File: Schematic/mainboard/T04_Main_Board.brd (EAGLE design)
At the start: 78.2 x 33.3 mm, 21 parts, among them IC1 7805DT, J1 AVR_SPI_PRG_6PTH, U1 ATMEGA328P_PDIP

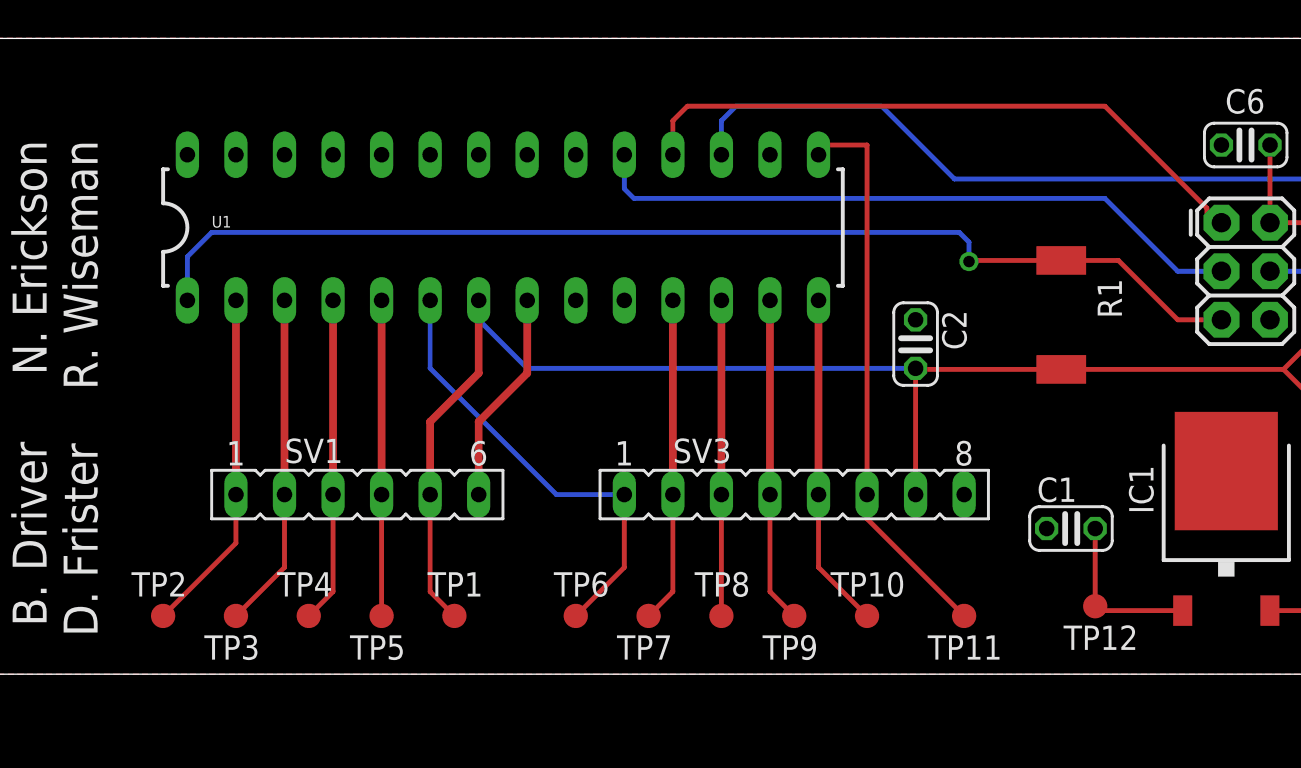
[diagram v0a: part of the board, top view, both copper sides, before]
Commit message: Mainboard update - Clock and bypass caps
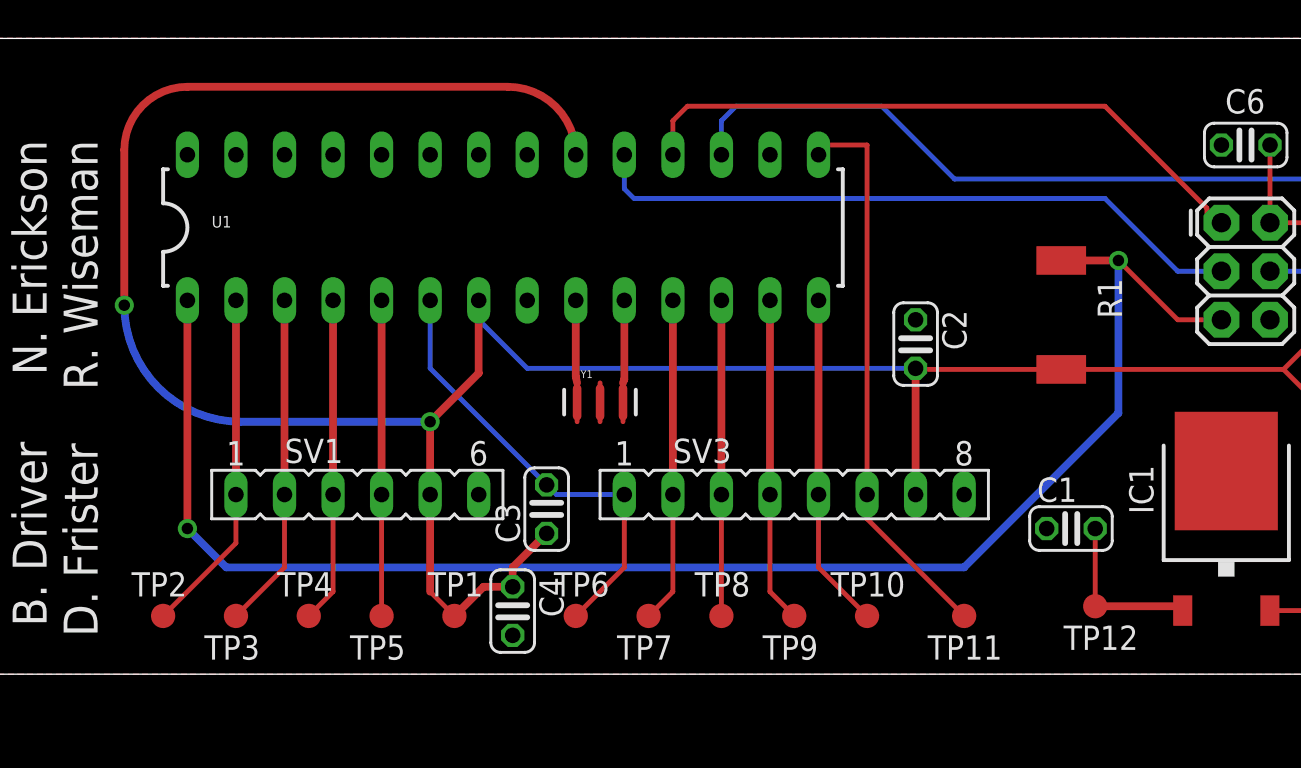
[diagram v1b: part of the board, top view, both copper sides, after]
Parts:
- added C3, C4: 0.1u, rcl:C025-024X044
- added Y1: 16MHZ, SparkFun-FreqCtrl:RESONATOR-SMD
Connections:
- new net N$1: U1.9, Y1.1
- new net N$2: U1.10, Y1.3
- new net N$3: Y1.2
- net +5V: now also C3.1, C4.1, U1.20
- net GND: now also C3.2, C4.2
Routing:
- net +5V: track 101.7 -> 162.0 mm, vias 0 -> 2
- net RESET: track 59.4 -> 82.5 mm, vias 1 -> 2
- net GND: track 10.7 -> 0.00 mm
- net N$2: track 0.00 -> 4.33 mm
- net N$1: track 0.00 -> 4.33 mm
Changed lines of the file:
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@@
 </element>
 <element name="U1" library="SparkFun-DigitalIC" package="DIL28-3" value="ATMEGA328P_PDIP" x="30.988" y="23.368"/>
+<element name="C3" library="rcl" package="C025-024X044" value="0.1u" x="33.274" y="8.636" rot="R90"/>
+<element name="C4" library="rcl" package="C025-024X044" value="0.1u" x="31.496" y="3.302" rot="R270"/>
+<element name="Y1" library="SparkFun-FreqCtrl" package="RESONATOR-SMD" value="16MHZ" x="36.068" y="14.224">
+<attribute name="PROD_ID" value="XTAL-08900" x="36.068" y="14.224" size="1.778" layer="27" display="off"/>
+</element>
 </elements>
 <signals>
@@
 <contactref element="J1" pad="6"/>
 <contactref element="C6" pad="2"/>
-<contactref element="SV1" pad="6"/>
 <contactref element="U1" pad="8"/>
 <contactref element="U1" pad="22"/>
-<contactref element="SV3" pad="8"/>
-<wire x1="29.718" y1="9.398" x2="29.464" y2="9.652" width="0.4064" layer="1"/>
-<wire x1="29.464" y1="9.652" x2="29.718" y2="9.906" width="0.4064" layer="1"/>
-<wire x1="29.718" y1="9.906" x2="29.718" y2="13.208" width="0.4064" layer="1"/>
-<wire x1="29.718" y1="13.208" x2="32.258" y2="15.748" width="0.4064" layer="1"/>
-<wire x1="32.258" y1="15.748" x2="32.258" y2="18.796" width="0.4064" layer="1"/>
 <polygon width="0.254" layer="1" isolate="0.3048">
 <vertex x="0" y="0"/>
@@
 <vertex x="78.232" y="0"/>
 </polygon>
+<contactref element="C3" pad="2"/>
+<contactref element="SV3" pad="8"/>
+<contactref element="C4" pad="2"/>
+<contactref element="SV1" pad="6"/>
 </signal>
 <signal name="+5V">
@@
 <contactref element="TP1" pad="TP"/>
 <contactref element="J1" pad="2"/>
-<contactref element="SV1" pad="5"/>
 <contactref element="C6" pad="1"/>
-<contactref element="SV3" pad="7"/>
 <contactref element="U1" pad="7"/>
-<wire x1="27.178" y1="9.398" x2="27.178" y2="13.208" width="0.4064" layer="1"/>
 <wire x1="27.178" y1="13.208" x2="29.718" y2="15.748" width="0.4064" layer="1"/>
 <wire x1="29.718" y1="15.748" x2="29.718" y2="19.558" width="0.4064" layer="1"/>
-<wire x1="27.178" y1="9.398" x2="27.178" y2="4.318" width="0.254" layer="1"/>
 <wire x1="27.178" y1="4.318" x2="28.448" y2="3.048" width="0.254" layer="1"/>
 <wire x1="60.198" y1="15.946" x2="71.826" y2="15.946" width="0.254" layer="1"/>
@@
 <wire x1="60.198" y1="15.946" x2="52.634" y2="15.946" width="0.254" layer="1"/>
 <wire x1="52.634" y1="15.946" x2="52.578" y2="16.002" width="0.254" layer="1"/>
-<wire x1="52.578" y1="9.398" x2="52.578" y2="16.002" width="0.254" layer="1"/>
 <wire x1="71.12" y1="27.686" x2="71.12" y2="24.384" width="0.254" layer="1"/>
 <wire x1="71.12" y1="24.384" x2="71.374" y2="24.13" width="0.254" layer="1"/>
@@
 <wire x1="32.258" y1="16.002" x2="29.718" y2="18.542" width="0.254" layer="16"/>
 <wire x1="29.718" y1="18.542" x2="29.718" y2="19.558" width="0.254" layer="16"/>
+<contactref element="C3" pad="1"/>
+<contactref element="SV3" pad="7"/>
+<contactref element="C4" pad="1"/>
+<contactref element="SV1" pad="5"/>
+<wire x1="52.578" y1="9.398" x2="52.578" y2="16.002" width="0.4064" layer="1"/>
+<wire x1="27.178" y1="13.208" x2="27.178" y2="9.398" width="0.4064" layer="1"/>
+<wire x1="27.178" y1="9.398" x2="27.178" y2="4.318" width="0.4064" layer="1"/>
+<wire x1="31.496" y1="4.572" x2="31.496" y2="5.588" width="0.4064" layer="1"/>
+<wire x1="31.496" y1="5.588" x2="33.274" y2="7.366" width="0.4064" layer="1"/>
+<wire x1="31.496" y1="4.572" x2="29.972" y2="4.572" width="0.4064" layer="1"/>
+<wire x1="29.972" y1="4.572" x2="28.448" y2="3.048" width="0.4064" layer="1"/>
+<contactref element="U1" pad="20"/>
+<wire x1="34.798" y1="27.178" x2="31.242" y2="30.734" width="0.4064" layer="1" curve="90"/>
+<wire x1="31.242" y1="30.734" x2="14.478" y2="30.734" width="0.4064" layer="1"/>
+<wire x1="14.478" y1="30.734" x2="11.176" y2="27.432" width="0.4064" layer="1" curve="90"/>
+<wire x1="11.176" y1="27.432" x2="11.176" y2="19.304" width="0.4064" layer="1"/>
+<via x="11.176" y="19.304" extent="1-16" drill="0.6" shape="square"/>
+<wire x1="11.176" y1="19.304" x2="17.272" y2="13.208" width="0.4064" layer="16" curve="90"/>
+<wire x1="17.272" y1="13.208" x2="27.178" y2="13.208" width="0.4064" layer="16"/>
+<via x="27.178" y="13.208" extent="1-16" drill="0.6" shape="square"/>
 </signal>
 <signal name="+12V">
@@
 <contactref element="IC1" pad="1"/>
 <contactref element="TP12" pad="TP"/>
-<wire x1="61.976" y1="7.62" x2="61.976" y2="3.328" width="0.254" layer="1"/>
-<wire x1="61.976" y1="3.328" x2="66.554" y2="3.328" width="0.254" layer="1"/>
-<wire x1="61.976" y1="3.328" x2="61.976" y2="3.556" width="0" layer="19" extent="1-1"/>
+<wire x1="61.976" y1="7.62" x2="61.976" y2="3.556" width="0.254" layer="1"/>
+<wire x1="61.976" y1="3.556" x2="61.976" y2="3.328" width="0.254" layer="1"/>
+<wire x1="61.976" y1="3.556" x2="66.326" y2="3.556" width="0.4064" layer="1"/>
+<wire x1="66.326" y1="3.556" x2="66.554" y2="3.328" width="0.4064" layer="1"/>
 </signal>
 <signal name="RESET">
 <contactref element="J1" pad="5"/>
+<wire x1="63.19" y1="21.646" x2="66.294" y2="18.542" width="0.254" layer="1"/>
+<wire x1="66.294" y1="18.542" x2="68.58" y2="18.542" width="0.254" layer="1"/>
 <contactref element="R1" pad="1"/>
 <contactref element="U1" pad="1"/>
-<wire x1="60.198" y1="21.646" x2="63.19" y2="21.646" width="0.254" layer="1"/>
-<wire x1="63.19" y1="21.646" x2="66.294" y2="18.542" width="0.254" layer="1"/>
-<wire x1="66.294" y1="18.542" x2="68.58" y2="18.542" width="0.254" layer="1"/>
-<wire x1="60.198" y1="21.646" x2="55.428" y2="21.646" width="0.254" layer="1"/>
-<wire x1="55.428" y1="21.646" x2="55.372" y2="21.59" width="0.254" layer="1"/>
-<via x="55.372" y="21.59" extent="1-16" drill="0.6"/>
-<wire x1="55.372" y1="21.59" x2="55.372" y2="22.606" width="0.254" layer="16"/>
-<wire x1="55.372" y1="22.606" x2="54.864" y2="23.114" width="0.254" layer="16"/>
-<wire x1="54.864" y1="23.114" x2="15.748" y2="23.114" width="0.254" layer="16"/>
-<wire x1="15.748" y1="23.114" x2="14.478" y2="21.844" width="0.254" layer="16"/>
-<wire x1="14.478" y1="21.844" x2="14.478" y2="19.558" width="0.254" layer="16"/>
+<via x="63.19" y="21.646" extent="1-16" drill="0.6" shape="square"/>
+<wire x1="63.19" y1="21.646" x2="63.19" y2="13.66" width="0.4064" layer="16"/>
+<wire x1="63.19" y1="13.66" x2="55.118" y2="5.588" width="0.4064" layer="16"/>
+<wire x1="55.118" y1="5.588" x2="16.51" y2="5.588" width="0.4064" layer="16"/>
+<wire x1="16.51" y1="5.588" x2="14.478" y2="7.62" width="0.4064" layer="16"/>
+<via x="14.478" y="7.62" extent="1-16" drill="0.6" shape="square"/>
+<wire x1="14.478" y1="7.62" x2="14.478" y2="19.558" width="0.4064" layer="1"/>
+<wire x1="60.198" y1="21.646" x2="63.19" y2="21.646" width="0.4064" layer="1"/>
 </signal>
 <signal name="ECHO1">
@@
 <wire x1="27.178" y1="16.002" x2="27.178" y2="19.558" width="0.254" layer="16"/>
 </signal>
+<signal name="N$1">
+<contactref element="Y1" pad="1"/>
+<contactref element="U1" pad="9"/>
+<wire x1="34.798" y1="19.558" x2="34.798" y2="15.564" width="0.4064" layer="1"/>
+<wire x1="34.798" y1="15.564" x2="34.868" y2="15.24" width="0.4064" layer="1"/>
+</signal>
+<signal name="N$2">
+<contactref element="Y1" pad="3"/>
+<contactref element="U1" pad="10"/>
+<wire x1="37.338" y1="19.558" x2="37.338" y2="15.424" width="0.4064" layer="1"/>
+<wire x1="37.338" y1="15.424" x2="37.268" y2="15.24" width="0.4064" layer="1"/>
+</signal>
+<signal name="N$3">
+<contactref element="Y1" pad="2"/>
+</signal>
 </signals>

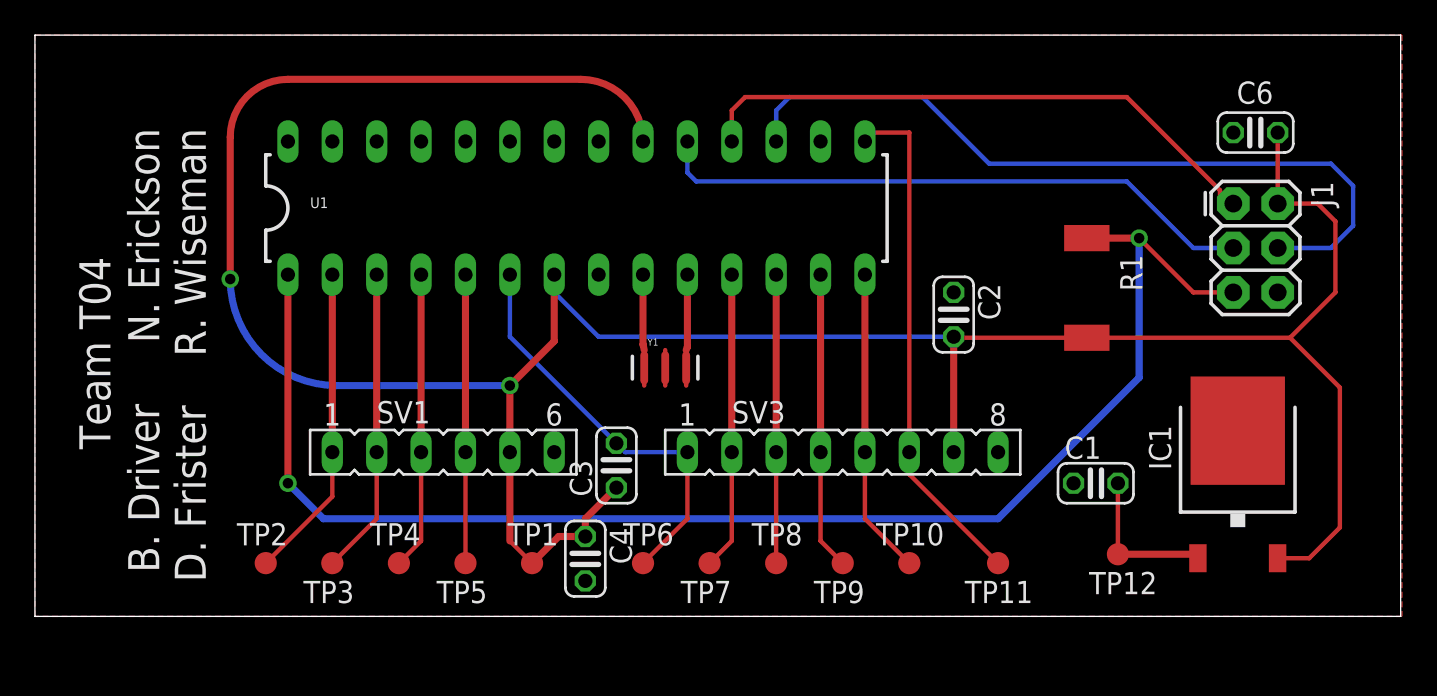
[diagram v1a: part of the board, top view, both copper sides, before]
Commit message: Mainboard - Added mounting holes
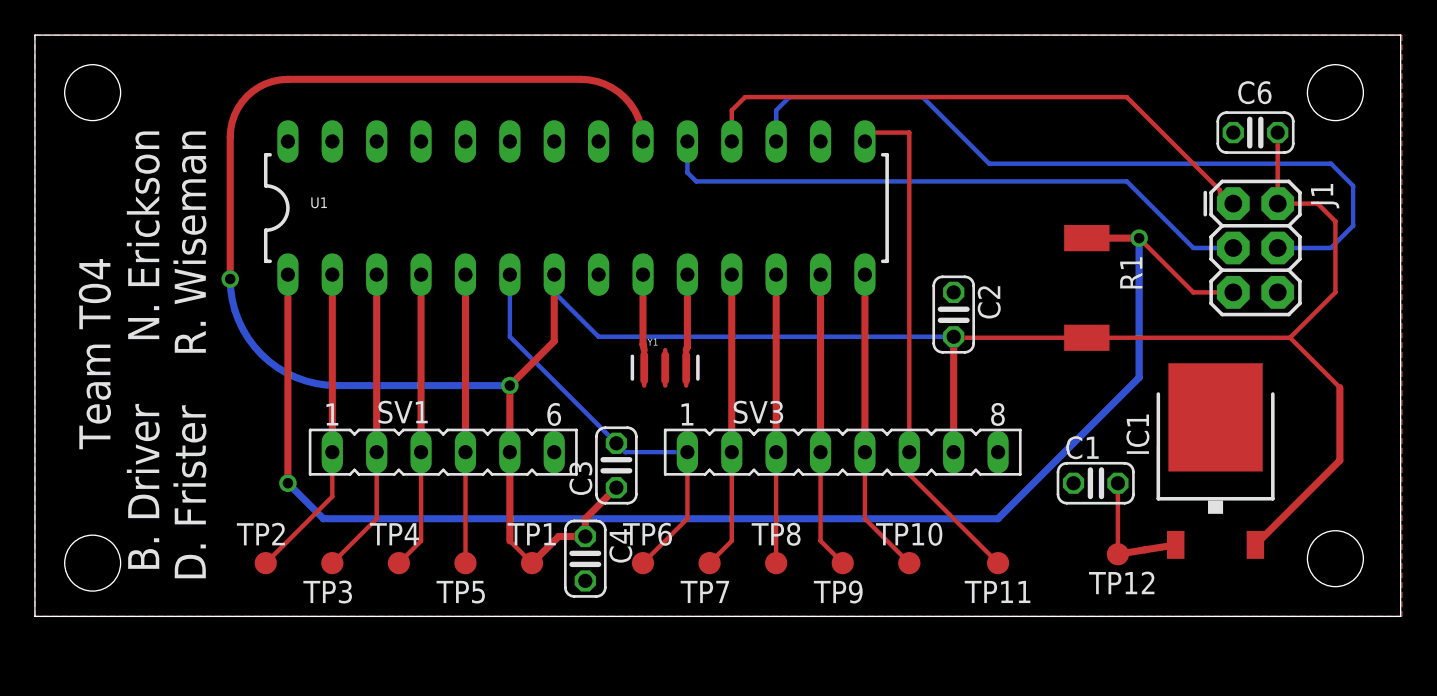
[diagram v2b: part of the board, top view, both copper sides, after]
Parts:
- moved IC1 1.48 mm to (67.6, 8.89)
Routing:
- net +12V: track 8.96 -> 7.64 mm
- net +5V: track 162.0 -> 160.7 mm
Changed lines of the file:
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@@
 <layer number="43" name="vRestrict" color="2" fill="10" visible="yes" active="yes"/>
 <layer number="44" name="Drills" color="7" fill="1" visible="no" active="yes"/>
-<layer number="45" name="Holes" color="7" fill="1" visible="no" active="yes"/>
+<layer number="45" name="Holes" color="7" fill="1" visible="yes" active="yes"/>
 <layer number="46" name="Milling" color="3" fill="1" visible="no" active="yes"/>
 <layer number="47" name="Measures" color="7" fill="1" visible="no" active="yes"/>
@@
 <text x="5.334" y="27.94" size="1.778" layer="25" rot="R270">B. Driver     N. Erickson
 D. Frister    R. Wiseman</text>
+<hole x="3.302" y="29.972" drill="3.2"/>
+<hole x="3.302" y="3.048" drill="3.2"/>
+<hole x="74.422" y="29.972" drill="3.2"/>
+<hole x="74.422" y="3.302" drill="3.2"/>
 </plain>
 <attributes>
@@
 <attribute name="VALUE" x="75.438" y="30.607" size="1.27" layer="27" ratio="10" rot="R180"/>
 </element>
-<element name="IC1" library="linear" package="TO252" value="7805DT" x="68.834" y="8.128" smashed="yes">
-<attribute name="NAME" x="65.024" y="8.382" size="1.27" layer="25" rot="R90"/>
-<attribute name="VALUE" x="73.914" y="5.588" size="1.27" layer="27" rot="R90"/>
+<element name="IC1" library="linear" package="TO252" value="7805DT" x="67.564" y="8.89" smashed="yes">
+<attribute name="NAME" x="63.754" y="9.144" size="1.27" layer="25" rot="R90"/>
+<attribute name="VALUE" x="72.644" y="6.35" size="1.27" layer="27" rot="R90"/>
 </element>
 <element name="J1" library="SparkFun-Connectors" package="2X3" value="AVR_SPI_PRG_6PTH" x="68.58" y="23.622" smashed="yes" rot="R270">
@@
 <wire x1="71.374" y1="24.13" x2="71.374" y2="23.876" width="0.254" layer="1"/>
 <wire x1="71.374" y1="23.876" x2="71.12" y2="23.622" width="0.254" layer="1"/>
-<wire x1="71.114" y1="3.328" x2="72.924" y2="3.328" width="0.254" layer="1"/>
-<wire x1="72.924" y1="3.328" x2="74.676" y2="5.08" width="0.254" layer="1"/>
-<wire x1="74.676" y1="5.08" x2="74.676" y2="13.096" width="0.254" layer="1"/>
 <wire x1="74.676" y1="13.096" x2="71.826" y2="15.946" width="0.254" layer="1"/>
 <wire x1="52.578" y1="16.002" x2="32.258" y2="16.002" width="0.254" layer="16"/>
@@
 <wire x1="17.272" y1="13.208" x2="27.178" y2="13.208" width="0.4064" layer="16"/>
 <via x="27.178" y="13.208" extent="1-16" drill="0.6" shape="square"/>
+<wire x1="74.676" y1="13.096" x2="74.676" y2="8.922" width="0.4064" layer="1"/>
+<wire x1="74.676" y1="8.922" x2="69.844" y2="4.09" width="0.4064" layer="1"/>
 </signal>
 <signal name="+12V">
@@
 <wire x1="61.976" y1="7.62" x2="61.976" y2="3.556" width="0.254" layer="1"/>
 <wire x1="61.976" y1="3.556" x2="61.976" y2="3.328" width="0.254" layer="1"/>
-<wire x1="61.976" y1="3.556" x2="66.326" y2="3.556" width="0.4064" layer="1"/>
-<wire x1="66.326" y1="3.556" x2="66.554" y2="3.328" width="0.4064" layer="1"/>
+<wire x1="61.976" y1="3.556" x2="63.532" y2="3.81" width="0.4064" layer="1"/>
+<wire x1="63.532" y1="3.81" x2="65.284" y2="4.09" width="0.4064" layer="1"/>
 </signal>
 <signal name="RESET">

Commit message: Fixed DRC errors on C3.
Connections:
- removed net GND: C1.1, C2.1, C3.2, C4.2, C6.2, IC1.3, J1.6, SV1.6, SV3.8, U1.22, U1.8
- removed net TRIG1: SV3.1, TP6.TP, U1.6
- new net S$1: C1.1, C2.1, C3.2, C4.2, C6.2, IC1.3, J1.6, SV1.6, SV3.1, SV3.8, TP6.TP, U1.22, U1.6, U1.8
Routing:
- net S$1: track 0.00 -> 30.7 mm
- net TRIG1: track 23.9 -> 0.00 mm
- added copper zone on layer 1, net S$1
- removed copper zone on layer 1, net GND
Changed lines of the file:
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@@
 </elements>
 <signals>
-<signal name="GND">
-<contactref element="IC1" pad="3"/>
-<contactref element="C1" pad="1"/>
-<contactref element="C2" pad="1"/>
-<contactref element="J1" pad="6"/>
-<contactref element="C6" pad="2"/>
-<contactref element="U1" pad="8"/>
-<contactref element="U1" pad="22"/>
-<polygon width="0.254" layer="1" isolate="0.3048">
-<vertex x="0" y="0"/>
-<vertex x="0" y="33.274"/>
-<vertex x="78.232" y="33.274"/>
-<vertex x="78.232" y="0"/>
-</polygon>
-<contactref element="C3" pad="2"/>
-<contactref element="SV3" pad="8"/>
-<contactref element="C4" pad="2"/>
-<contactref element="SV1" pad="6"/>
-</signal>
 <signal name="+5V">
 <contactref element="C2" pad="2"/>
@@
 <wire x1="47.498" y1="5.588" x2="50.038" y2="3.048" width="0.254" layer="1"/>
 </signal>
-<signal name="TRIG1">
+<signal name="S$1">
+<contactref element="U1" pad="6"/>
+<wire x1="27.178" y1="16.002" x2="27.178" y2="19.558" width="0.254" layer="16"/>
+<contactref element="IC1" pad="3"/>
+<contactref element="C1" pad="1"/>
+<contactref element="C2" pad="1"/>
+<contactref element="J1" pad="6"/>
+<contactref element="C6" pad="2"/>
+<contactref element="U1" pad="8"/>
+<contactref element="U1" pad="22"/>
+<polygon width="0.254" layer="1" isolate="0.3048">
+<vertex x="0" y="0"/>
+<vertex x="0" y="33.274"/>
+<vertex x="78.232" y="33.274"/>
+<vertex x="78.232" y="0"/>
+</polygon>
+<contactref element="C3" pad="2"/>
+<contactref element="SV3" pad="8"/>
+<contactref element="C4" pad="2"/>
+<contactref element="SV1" pad="6"/>
+<wire x1="33.274" y1="9.906" x2="33.274" y2="14.732" width="0.4064" layer="16"/>
+<wire x1="33.274" y1="14.732" x2="33.02" y2="14.986" width="0.4064" layer="16"/>
+<wire x1="33.02" y1="14.986" x2="27.432" y2="14.986" width="0.4064" layer="16"/>
+<wire x1="27.432" y1="14.986" x2="27.178" y2="15.24" width="0.4064" layer="16"/>
+<wire x1="27.178" y1="15.24" x2="27.178" y2="19.558" width="0.4064" layer="16"/>
 <contactref element="SV3" pad="1"/>
-<contactref element="U1" pad="6"/>
 <contactref element="TP6" pad="TP"/>
 <wire x1="37.338" y1="9.398" x2="37.338" y2="5.588" width="0.254" layer="1"/>
 <wire x1="37.338" y1="5.588" x2="34.798" y2="3.048" width="0.254" layer="1"/>
-<wire x1="37.338" y1="9.398" x2="33.782" y2="9.398" width="0.254" layer="16"/>
-<wire x1="33.782" y1="9.398" x2="27.178" y2="16.002" width="0.254" layer="16"/>
-<wire x1="27.178" y1="16.002" x2="27.178" y2="19.558" width="0.254" layer="16"/>
+<wire x1="33.274" y1="9.906" x2="33.782" y2="9.398" width="0.4064" layer="16"/>
+<wire x1="33.782" y1="9.398" x2="37.338" y2="9.398" width="0.4064" layer="16"/>
 </signal>
 <signal name="N$1">
